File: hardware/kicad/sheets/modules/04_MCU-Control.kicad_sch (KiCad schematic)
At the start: 0 parts

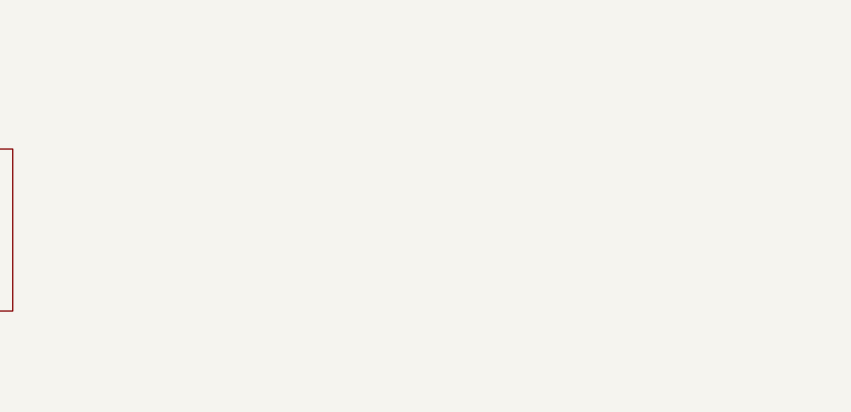
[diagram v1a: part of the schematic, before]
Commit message: better sheet nesting for power rails
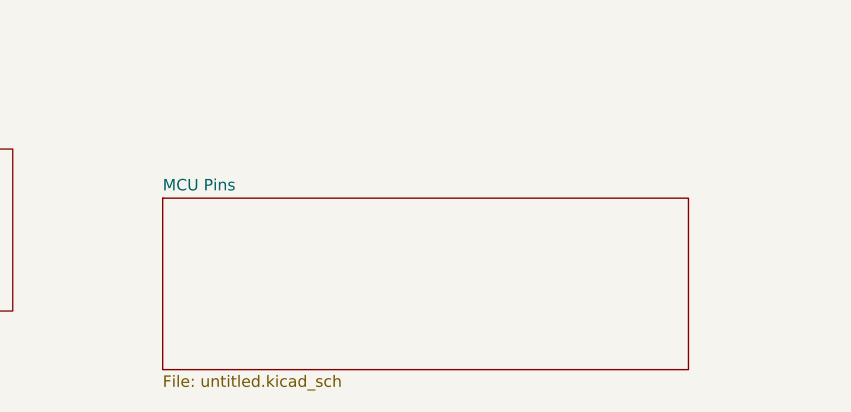
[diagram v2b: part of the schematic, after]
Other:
- added sheet MCU Pins (untitled.kicad_sch)
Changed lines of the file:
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@@
+	)
+	(sheet
+		(at 200.66 124.46)
+		(size 58.42 19.05)
+		(exclude_from_sim no)
+		(in_bom yes)
+		(on_board yes)
+		(dnp no)
+		(fields_autoplaced yes)
+		(stroke
+			(width 0.1524)
+			(type solid)
+		)
+		(fill
+			(color 0 0 0 0.0000)
+		)
+		(property "Sheetname" "MCU Pins"
+			(at 200.66 123.7484 0)
+			(effects
+				(font
+					(size 1.27 1.27)
+				)
+				(justify left bottom)
+			)
+		)
+		(property "Sheetfile" "untitled.kicad_sch"
+			(at 200.66 144.0946 0)
+			(effects
+				(font
+					(size 1.27 1.27)
+				)
+				(justify left top)
+			)
+		)
+		(instances
+			(project "svea_powerboard_rev3"
+				(path "/3f85abf4-0b95-4c4a-b7e9-06f59ca1ea3d/5c2e021f-c2d4-49e2-8c36-9a64f1f12004"
+					(page "30")
+				)
+			)
+		)
 	)
 	(sheet

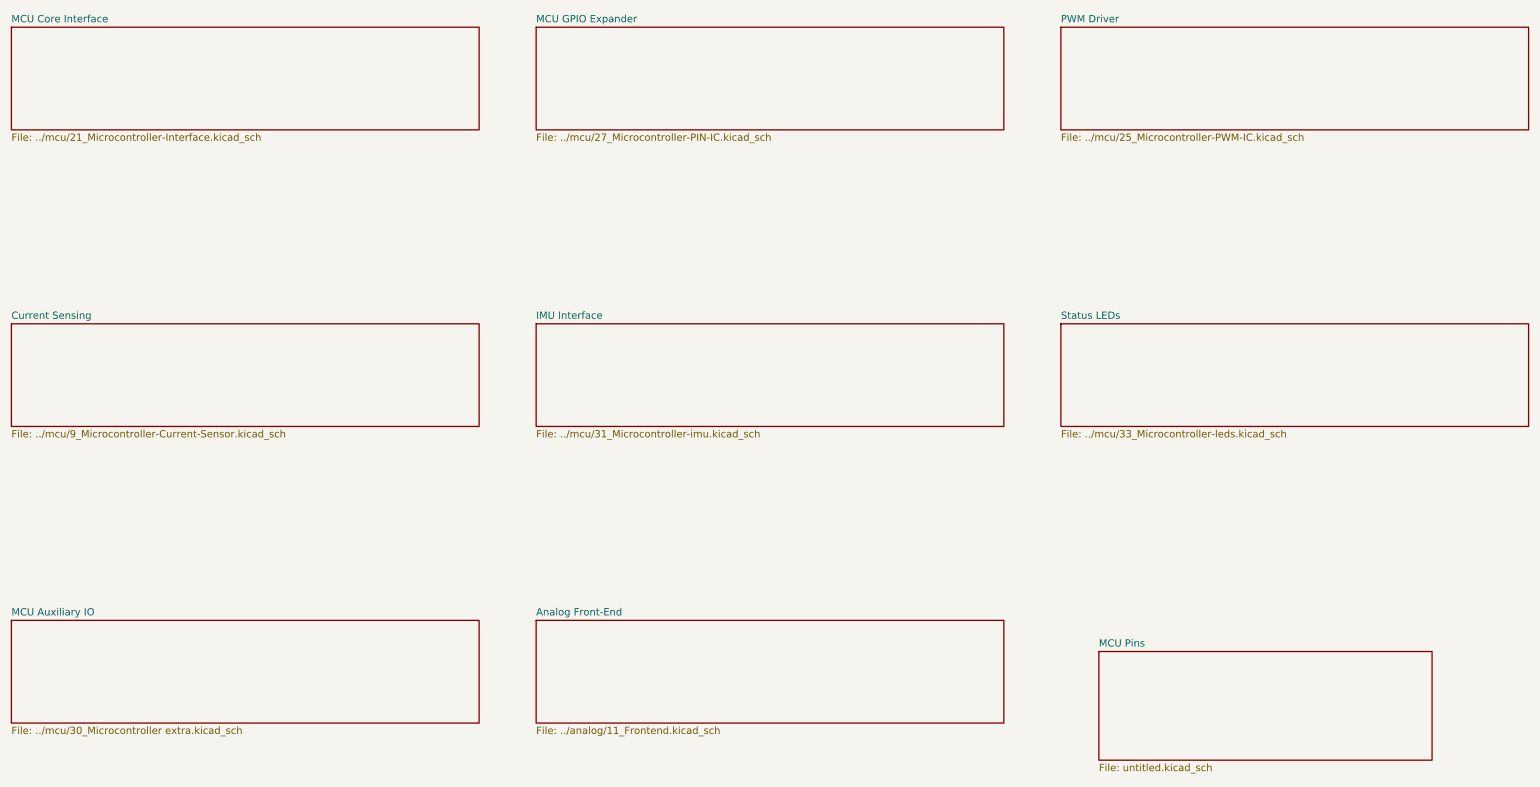
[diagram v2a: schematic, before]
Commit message: netties and better sheet nesting for servo connectors
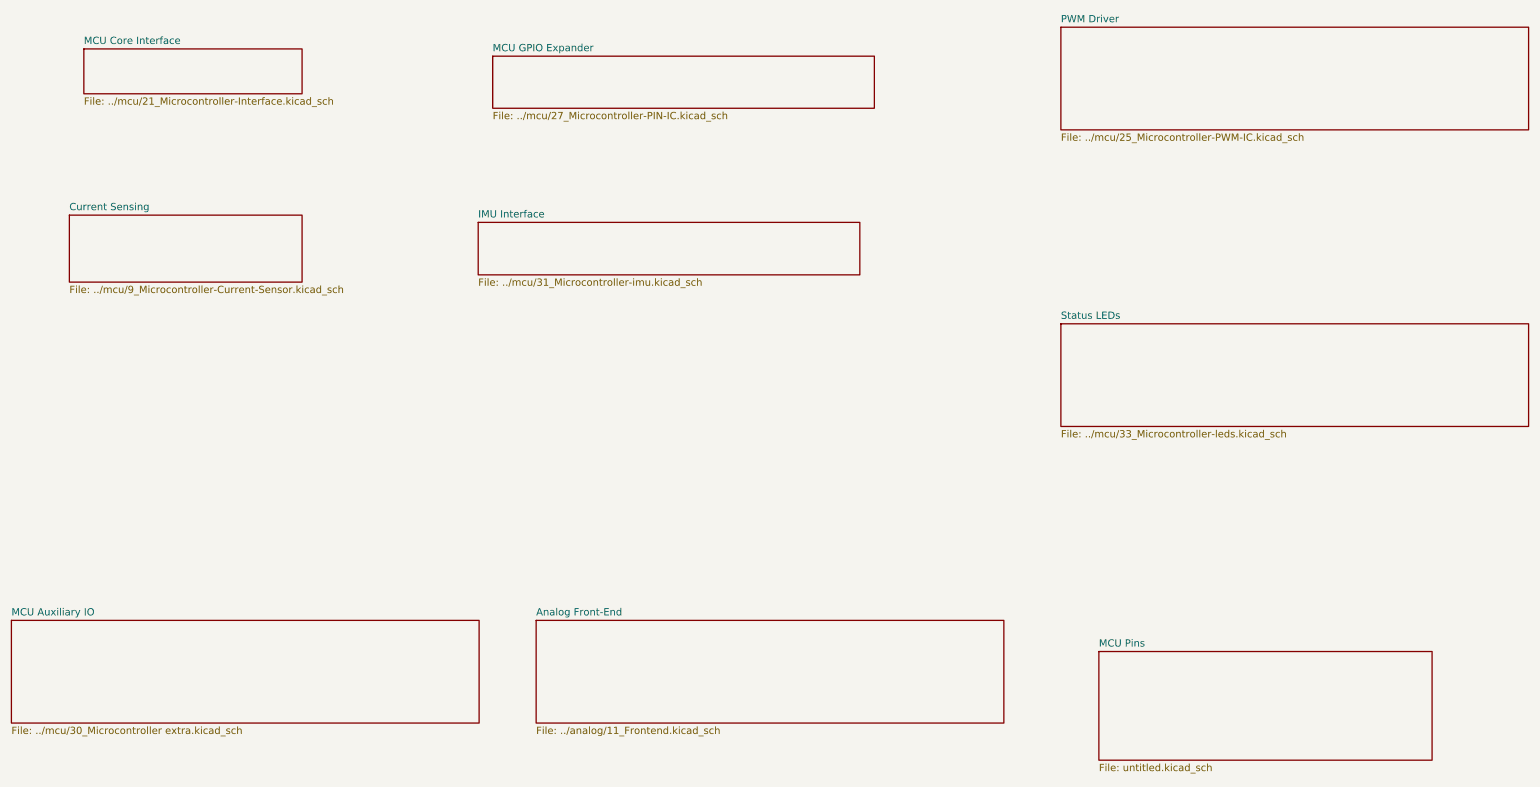
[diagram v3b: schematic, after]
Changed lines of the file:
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@@
 	)
 	(sheet
-		(at 10 15)
-		(size 82 18)
+		(at 22.7 18.81)
+		(size 38.26 7.86)
 		(exclude_from_sim no)
 		(in_bom yes)
@@
 		)
 		(property "Sheetname" "MCU Core Interface"
-			(at 10 14.2884 0)
+			(at 22.7 18.0984 0)
 			(effects
 				(font
@@
 		)
 		(property "Sheetfile" "../mcu/21_Microcontroller-Interface.kicad_sch"
-			(at 10 33.5846 0)
+			(at 22.7 27.2546 0)
 			(effects
 				(font
@@
 	)
 	(sheet
-		(at 102 15)
-		(size 82 18)
+		(at 94.38 20.08)
+		(size 66.91 9.13)
 		(exclude_from_sim no)
 		(in_bom yes)
@@
 		)
 		(property "Sheetname" "MCU GPIO Expander"
-			(at 102 14.2884 0)
+			(at 94.38 19.3684 0)
 			(effects
 				(font
@@
 		)
 		(property "Sheetfile" "../mcu/27_Microcontroller-PIN-IC.kicad_sch"
-			(at 102 33.5846 0)
+			(at 94.38 29.7946 0)
 			(effects
 				(font
@@
 	)
 	(sheet
-		(at 10 67)
-		(size 82 18)
+		(at 20.16 47.95)
+		(size 40.8 11.74)
 		(exclude_from_sim no)
 		(in_bom yes)
@@
 		)
 		(property "Sheetname" "Current Sensing"
-			(at 10 66.2884 0)
+			(at 20.16 47.2384 0)
 			(effects
 				(font
@@
 		)
 		(property "Sheetfile" "../mcu/9_Microcontroller-Current-Sensor.kicad_sch"
-			(at 10 85.5846 0)
+			(at 20.16 60.2746 0)
 			(effects
 				(font
@@
 	)
 	(sheet
-		(at 102 67)
-		(size 82 18)
+		(at 91.84 49.22)
+		(size 66.91 9.2)
 		(exclude_from_sim no)
 		(in_bom yes)
@@
 		)
 		(property "Sheetname" "IMU Interface"
-			(at 102 66.2884 0)
+			(at 91.84 48.5084 0)
 			(effects
 				(font
@@
 		)
 		(property "Sheetfile" "../mcu/31_Microcontroller-imu.kicad_sch"
-			(at 102 85.5846 0)
+			(at 91.84 59.0046 0)
 			(effects
 				(font

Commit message: more sheet simplfiication and pre simpler 12v sym
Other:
- removed sheet Current Sensing
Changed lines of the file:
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@@
-	)
-	(sheet
-		(at 20.16 47.95)
-		(size 40.8 11.74)
-		(exclude_from_sim no)
-		(in_bom yes)
-		(on_board yes)
-		(dnp no)
-		(fields_autoplaced yes)
-		(stroke
-			(width 0)
-			(type solid)
-		)
-		(fill
-			(color 0 0 0 0.0000)
-		)
-		(property "Sheetname" "Current Sensing"
-			(at 20.16 47.2384 0)
-			(effects
-				(font
-					(size 1.27 1.27)
-				)
-				(justify left bottom)
-			)
-		)
-		(property "Sheetfile" "../mcu/9_Microcontroller-Current-Sensor.kicad_sch"
-			(at 20.16 60.2746 0)
-			(effects
-				(font
-					(size 1.27 1.27)
-				)
-				(justify left top)
-			)
-		)
 	)
 	(sheet

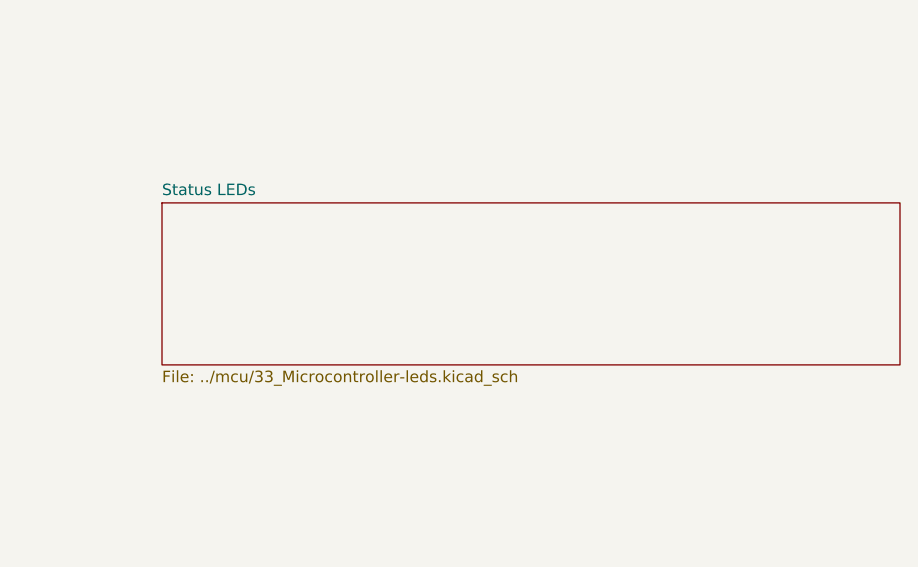
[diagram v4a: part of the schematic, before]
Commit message: moved servos to root
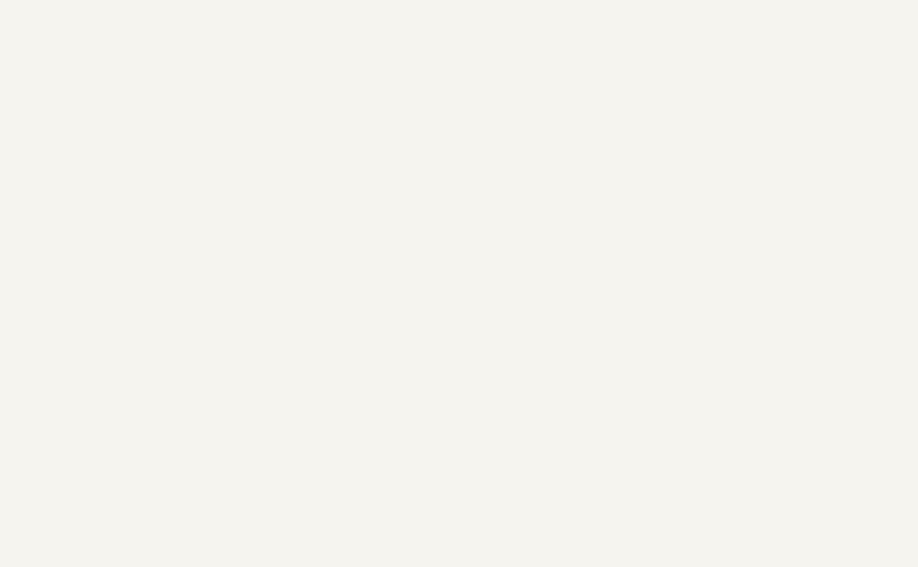
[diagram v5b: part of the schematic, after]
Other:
- removed sheet Status LEDs
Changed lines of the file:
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@@
-	)
-	(sheet
-		(at 194 67)
-		(size 82 18)
-		(exclude_from_sim no)
-		(in_bom yes)
-		(on_board yes)
-		(dnp no)
-		(fields_autoplaced yes)
-		(stroke
-			(width 0)
-			(type solid)
-		)
-		(fill
-			(color 0 0 0 0.0000)
-		)
-		(property "Sheetname" "Status LEDs"
-			(at 194 66.2884 0)
-			(effects
-				(font
-					(size 1.27 1.27)
-				)
-				(justify left bottom)
-			)
-		)
-		(property "Sheetfile" "../mcu/33_Microcontroller-leds.kicad_sch"
-			(at 194 85.5846 0)
-			(effects
-				(font
-					(size 1.27 1.27)
-				)
-				(justify left top)
-			)
-		)
 	)
 	(sheet

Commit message: various improvements
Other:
- removed sheet PWM Driver
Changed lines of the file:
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@@
-	)
-	(sheet
-		(at 194 15)
-		(size 82 18)
-		(exclude_from_sim no)
-		(in_bom yes)
-		(on_board yes)
-		(dnp no)
-		(fields_autoplaced yes)
-		(stroke
-			(width 0)
-			(type solid)
-		)
-		(fill
-			(color 0 0 0 0.0000)
-		)
-		(property "Sheetname" "PWM Driver"
-			(at 194 14.2884 0)
-			(effects
-				(font
-					(size 1.27 1.27)
-				)
-				(justify left bottom)
-			)
-		)
-		(property "Sheetfile" "../mcu/25_Microcontroller-PWM-IC.kicad_sch"
-			(at 194 33.5846 0)
-			(effects
-				(font
-					(size 1.27 1.27)
-				)
-				(justify left top)
-			)
-		)
 	)
 	(sheet

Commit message: current sensing on the servos and cleaning up empty sheets
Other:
- removed sheet Analog Front-End
- removed sheet IMU Interface
- removed sheet MCU Auxiliary IO
- removed sheet MCU Core Interface
- removed sheet MCU GPIO Expander
- removed sheet MCU Pins
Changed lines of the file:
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@@
 		(date "2026-02-16")
 	)
-	(sheet
-		(at 200.66 124.46)
-		(size 58.42 19.05)
-		(exclude_from_sim no)
-		(in_bom yes)
-		(on_board yes)
-		(dnp no)
-		(fields_autoplaced yes)
-		(stroke
-			(width 0.1524)
-			(type solid)
-		)
-		(fill
-			(color 0 0 0 0.0000)
-		)
-		(property "Sheetname" "MCU Pins"
-			(at 200.66 123.7484 0)
-			(effects
-				(font
-					(size 1.27 1.27)
-				)
-				(justify left bottom)
-			)
-		)
-		(property "Sheetfile" "untitled.kicad_sch"
-			(at 200.66 144.0946 0)
-			(effects
-				(font
-					(size 1.27 1.27)
-				)
-				(justify left top)
-			)
-		)
-		(instances
-			(project "svea_powerboard_rev3"
-				(path "/3f85abf4-0b95-4c4a-b7e9-06f59ca1ea3d/5c2e021f-c2d4-49e2-8c36-9a64f1f12004"
-					(page "30")
-				)
-			)
-		)
-	)
-	(sheet
-		(at 22.7 18.81)
-		(size 38.26 7.86)
-		(exclude_from_sim no)
-		(in_bom yes)
-		(on_board yes)
-		(dnp no)
-		(fields_autoplaced yes)
-		(stroke
-			(width 0)
-			(type solid)
-		)
-		(fill
-			(color 0 0 0 0.0000)
-		)
-		(property "Sheetname" "MCU Core Interface"
-			(at 22.7 18.0984 0)
-			(effects
-				(font
-					(size 1.27 1.27)
-				)
-				(justify left bottom)
-			)
-		)
-		(property "Sheetfile" "../mcu/21_Microcontroller-Interface.kicad_sch"
-			(at 22.7 27.2546 0)
-			(effects
-				(font
-					(size 1.27 1.27)
-				)
-				(justify left top)
-			)
-		)
-	)
-	(sheet
-		(at 94.38 20.08)
-		(size 66.91 9.13)
-		(exclude_from_sim no)
-		(in_bom yes)
-		(on_board yes)
-		(dnp no)
-		(fields_autoplaced yes)
-		(stroke
-			(width 0)
-			(type solid)
-		)
-		(fill
-			(color 0 0 0 0.0000)
-		)
-		(property "Sheetname" "MCU GPIO Expander"
-			(at 94.38 19.3684 0)
-			(effects
-				(font
-					(size 1.27 1.27)
-				)
-				(justify left bottom)
-			)
-		)
-		(property "Sheetfile" "../mcu/27_Microcontroller-PIN-IC.kicad_sch"
-			(at 94.38 29.7946 0)
-			(effects
-				(font
-					(size 1.27 1.27)
-				)
-				(justify left top)
-			)
-		)
-	)
-	(sheet
-		(at 91.84 49.22)
-		(size 66.91 9.2)
-		(exclude_from_sim no)
-		(in_bom yes)
-		(on_board yes)
-		(dnp no)
-		(fields_autoplaced yes)
-		(stroke
-			(width 0)
-			(type solid)
-		)
-		(fill
-			(color 0 0 0 0.0000)
-		)
-		(property "Sheetname" "IMU Interface"
-			(at 91.84 48.5084 0)
-			(effects
-				(font
-					(size 1.27 1.27)
-				)
-				(justify left bottom)
-			)
-		)
-		(property "Sheetfile" "../mcu/31_Microcontroller-imu.kicad_sch"
-			(at 91.84 59.0046 0)
-			(effects
-				(font
-					(size 1.27 1.27)
-				)
-				(justify left top)
-			)
-		)
-	)
-	(sheet
-		(at 10 119)
-		(size 82 18)
-		(exclude_from_sim no)
-		(in_bom yes)
-		(on_board yes)
-		(dnp no)
-		(fields_autoplaced yes)
-		(stroke
-			(width 0)
-			(type solid)
-		)
-		(fill
-			(color 0 0 0 0.0000)
-		)
-		(property "Sheetname" "MCU Auxiliary IO"
-			(at 10 118.2884 0)
-			(effects
-				(font
-					(size 1.27 1.27)
-				)
-				(justify left bottom)
-			)
-		)
-		(property "Sheetfile" "../mcu/30_Microcontroller extra.kicad_sch"
-			(at 10 137.5846 0)
-			(effects
-				(font
-					(size 1.27 1.27)
-				)
-				(justify left top)
-			)
-		)
-	)
-	(sheet
-		(at 102 119)
-		(size 82 18)
-		(exclude_from_sim no)
-		(in_bom yes)
-		(on_board yes)
-		(dnp no)
-		(fields_autoplaced yes)
-		(stroke
-			(width 0)
-			(type solid)
-		)
-		(fill
-			(color 0 0 0 0.0000)
-		)
-		(property "Sheetname" "Analog Front-End"
-			(at 102 118.2884 0)
-			(effects
-				(font
-					(size 1.27 1.27)
-				)
-				(justify left bottom)
-			)
-		)
-		(property "Sheetfile" "../analog/11_Frontend.kicad_sch"
-			(at 102 137.5846 0)
-			(effects
-				(font
-					(size 1.27 1.27)
-				)
-				(justify left top)
-			)
-		)
-	)
 )
